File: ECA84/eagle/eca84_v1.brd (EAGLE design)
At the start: 223 x 127 mm, 186 parts

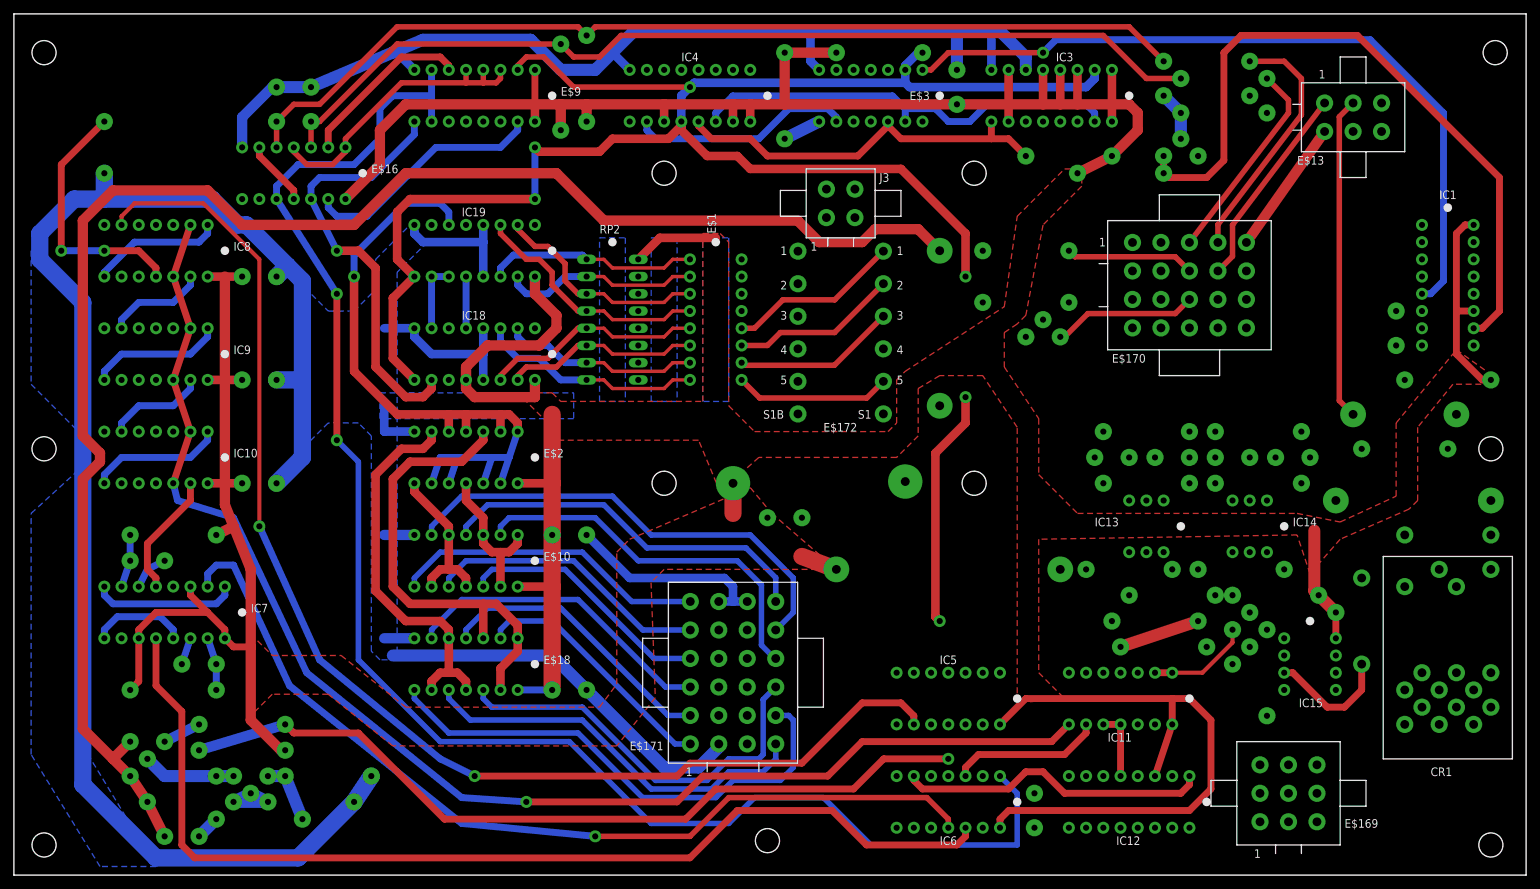
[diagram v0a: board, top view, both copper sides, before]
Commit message: casi todas las pistas bottom, falta poligono
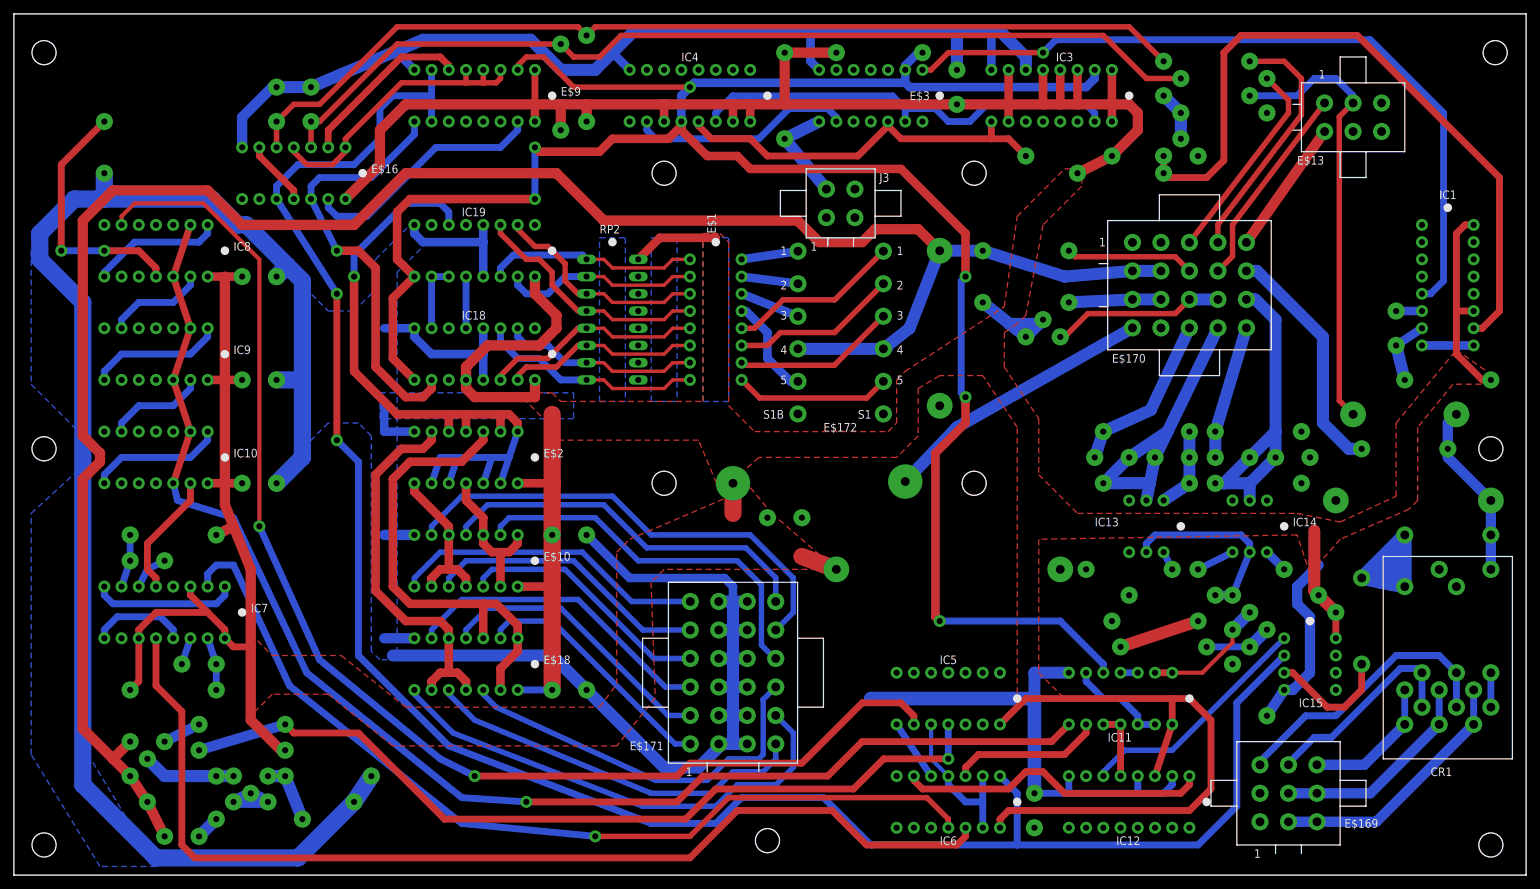
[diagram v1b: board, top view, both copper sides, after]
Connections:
- new net S$100: E$104.P$1, E$105.P$1, E$108.P$1
- new net S$101: E$111.P$1, E$112.P$1
- new net S$102: CR1.P$11, CR1.P$5, E$169.P$7
- new net S$103: CR1.P$2, CR1.P$8, E$169.P$5, E$169.P$6
- new net S$104: CR1.P$1, CR1.P$7, E$169.P$9
- new net S$105: CR1.P$10, CR1.P$4, E$169.P$8
- new net S$106: CR1.P$16, E$139.P$1, E$158.P$1, E$159.P$1, E$160.P$1
- new net S$107: CR1.P$13, E$156.P$1, E$157.P$1
- new net S$108: E$102.P$1, E$103.P$1, E$115.P$1, E$117.P$1, E$13.P$4, E$143.P$1, E$147.P$1, E$161.P$1, E$163.P$1, E$77.P$1, IC1.P$8, IC1.P$9, IC11.P$7, IC12.P$2, IC12.P$4, IC12.P$8, IC13.P$4, IC14.P$4, IC15.P$4, IC5.P$7, IC6.P$7, J3.P$4
- new net S$109: E$135.P$1, E$137.P$1, IC1.P$7
- new net S$110: E$134.P$1, E$170.P$18
- new net S$111: E$131.P$1, E$132.P$1, E$133.P$1, IC14.P$1
- new net S$112: E$123.P$1, E$126.P$1, E$127.P$1, IC13.P$1
- new net S$113: E$119.P$1, E$120.P$1, E$170.P$12
- new net S$114: E$144.P$1, E$170.P$2, E$170.P$6, E$172.P$7, E$172.P$8, E$34.P$1, E$37.P$1, E$38.P$1, E$39.P$1, E$84.P$1
- new net S$115: E$1.P$16, E$172.P$1
- new net S$116: E$1.P$15, E$172.P$3
- new net S$117: E$1.P$14, E$172.P$5
- new net S$118: E$1.P$13, E$172.P$9
- new net S$119: E$15.P$1, E$170.P$4
- new net S$120: E$118.P$1, E$121.P$1, E$122.P$1, E$170.P$16, IC13.P$2
- new net S$121: E$124.P$1, E$125.P$1, E$170.P$20
- new net S$122: E$170.P$3, E$170.P$7, E$87.P$1
- new net S$92: E$16.P$10, E$56.P$1, E$57.P$1, E$9.P$10, E$9.P$7, IC15.P$2, IC6.P$1
- new net S$93: IC11.P$12, IC11.P$13, IC11.P$6
- new net S$94: IC11.P$3, IC11.P$4
- new net S$95: CR1.P$12, CR1.P$6
- new net S$96: E$116.P$1, IC13.P$6
- new net S$97: E$136.P$1, IC1.P$6
- new net S$98: E$113.P$1, E$114.P$1, IC13.P$5, IC14.P$5
- new net S$99: E$154.P$1, IC14.P$6
- net S$13: now also E$86.P$1, E$88.P$1, E$90.P$1; no longer E$144.P$1, E$34.P$1, E$37.P$1, E$38.P$1, E$39.P$1
- net S$14: now also CR1.P$3, CR1.P$9, E$169.P$2, E$169.P$3; no longer E$103.P$1, E$117.P$1, E$143.P$1, E$161.P$1, E$163.P$1, E$77.P$1, IC1.P$8, IC1.P$9, IC13.P$4, IC5.P$7, IC6.P$7
- net S$49: now also E$107.P$1
- net S$51: now also E$128.P$1, E$129.P$1, E$130.P$1, E$170.P$19, IC14.P$2; no longer E$164.P$1, E$165.P$1
- net S$65: now also E$164.P$1, E$165.P$1, IC11.P$5
- net S$67: now also J3.P$3
- net S$69: now also E$171.P$8, E$18.P$8; no longer E$16.P$10, E$56.P$1, E$57.P$1, E$9.P$10, E$9.P$7, IC15.P$2, IC6.P$1
- net S$78: now also E$170.P$15
- net S$79: now also E$142.P$1
- net S$86: now also IC12.P$6, IC15.P$1; no longer E$171.P$12, E$18.P$12
- net S$91: now also E$171.P$12, E$18.P$12; no longer E$171.P$8, E$18.P$8
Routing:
- net S$114: track 0.00 -> 304.2 mm
- net S$92: track 0.00 -> 292.1 mm
- net S$13: track 240.5 -> 16.9 mm
- net S$69: track 235.2 -> 72.0 mm
- net S$108: track 0.00 -> 114.9 mm
- net S$65: track 238.3 -> 319.8 mm
- net S$120: track 0.00 -> 46.8 mm
- net S$102: track 0.00 -> 42.1 mm
- net GND: track 328.4 -> 370.4 mm
- net S$119: track 0.00 -> 40.8 mm
- net S$107: track 0.00 -> 38.4 mm
- net S$14: track 0.00 -> 38.3 mm
- net S$110: track 0.00 -> 35.3 mm
- net S$103: track 0.00 -> 31.5 mm
- net S$105: track 0.00 -> 31.1 mm
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
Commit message: Terminado poligono bottom
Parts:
- renumbered E$101 to GND
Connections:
- net S$120 renamed GRUPO1
- net S$51 renamed GRUPO2
- removed net S$108: E$102.P$1, E$103.P$1, E$115.P$1, E$117.P$1, E$13.P$4, E$143.P$1, E$147.P$1, E$161.P$1, E$163.P$1, E$77.P$1, IC1.P$8, IC1.P$9, IC11.P$7, IC12.P$2, IC12.P$4, IC12.P$8, IC13.P$4, IC14.P$4, IC15.P$4, IC5.P$7, IC6.P$7, J3.P$4
- removed net S$63: IC18.P$13, IC18.P$4, IC18.P$8, IC19.P$13, IC19.P$4, IC19.P$8
- removed net S$64: E$16.P$7, E$3.P$7, E$64.P$1, E$65.P$1, E$71.P$1, E$9.P$8, IC3.P$6, IC3.P$8, IC4.P$8
- net GND: now also E$102.P$1, E$103.P$1, E$115.P$1, E$117.P$1, E$13.P$4, E$143.P$1, E$147.P$1, E$16.P$7, E$161.P$1, E$163.P$1, E$166.P$1, E$3.P$7, E$64.P$1, E$65.P$1, E$71.P$1, E$77.P$1, E$9.P$8, GND.P$1, IC1.P$8, IC1.P$9, IC11.P$7, IC12.P$2, IC12.P$4, IC12.P$8, IC13.P$4, IC14.P$4, IC15.P$4, IC18.P$13, IC18.P$4, IC18.P$8, IC19.P$13, IC19.P$4, IC19.P$8, IC3.P$6, IC3.P$8, IC4.P$8, IC5.P$7, IC6.P$7, J3.P$4
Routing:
- net GND: track 370.4 -> 969.1 mm
- net S$64: track 156.5 -> 0.00 mm
- net S$108: track 114.9 -> 0.00 mm
- net S$63: track 44.1 -> 0.00 mm
- net S$111: track 0.00 -> 13.7 mm
- net S$101: track 0.00 -> 4.58 mm
- net S$88: track 42.2 -> 41.7 mm
- net S$87: track 46.6 -> 46.1 mm
- added copper zone on layer 16, net GRUPO1
- added copper zone on layer 16, net GRUPO2
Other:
- board text added: "PIELTEX 2021 TEPETZINGO"
